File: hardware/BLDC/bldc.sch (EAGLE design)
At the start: 84 parts, among them J1 PWR_2_XT30PW-M, J2 LINEAR_3_JST_PH_RA, J3 LINEAR_8_JST_PH_RA, U1 MA702, U10 MCP2542FD, U11 LDFM33PUR, U2 DRV8323RS, U3 TPN7R006PL, U4 TPN7R006PL, U5 TPN7R006PL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

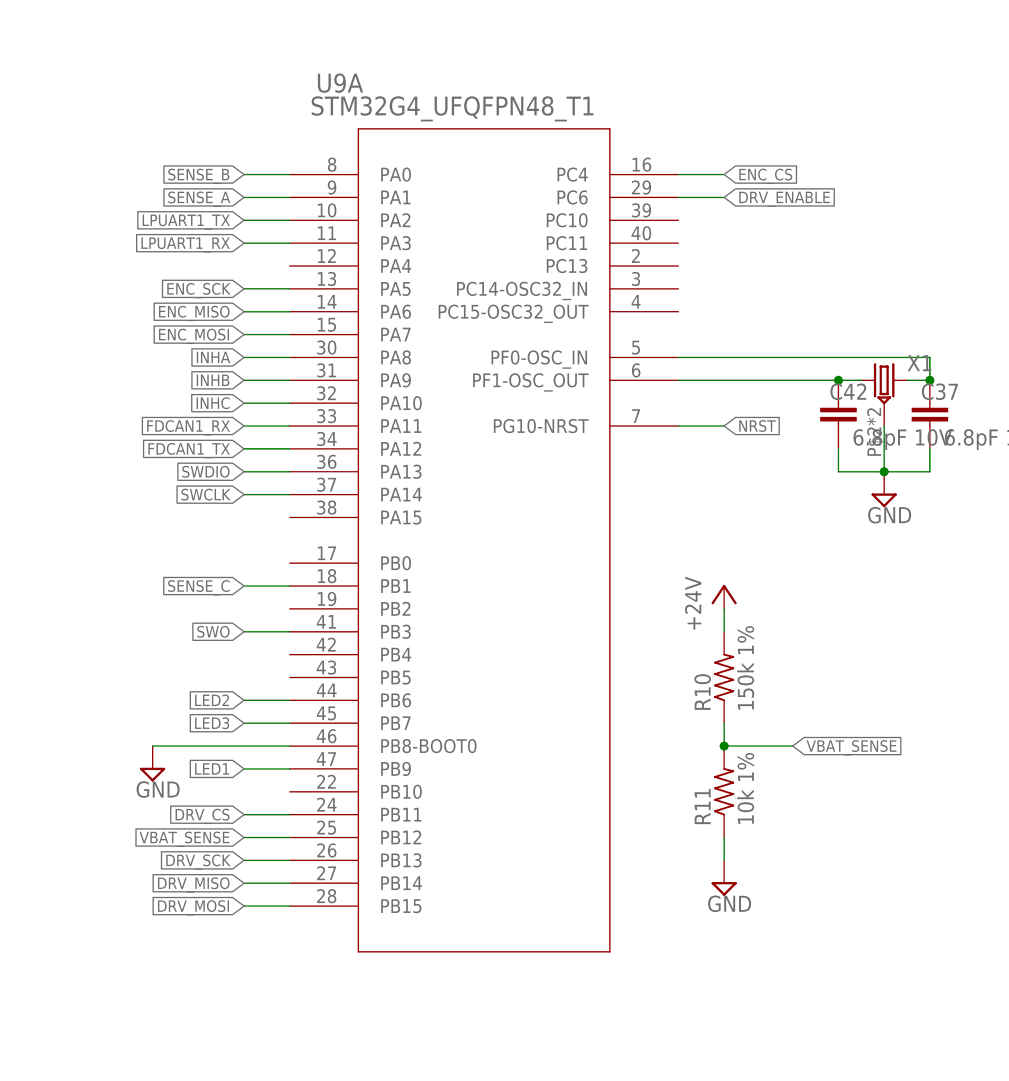
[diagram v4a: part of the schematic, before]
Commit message: SPI2>SPI3. Added cap on nRST
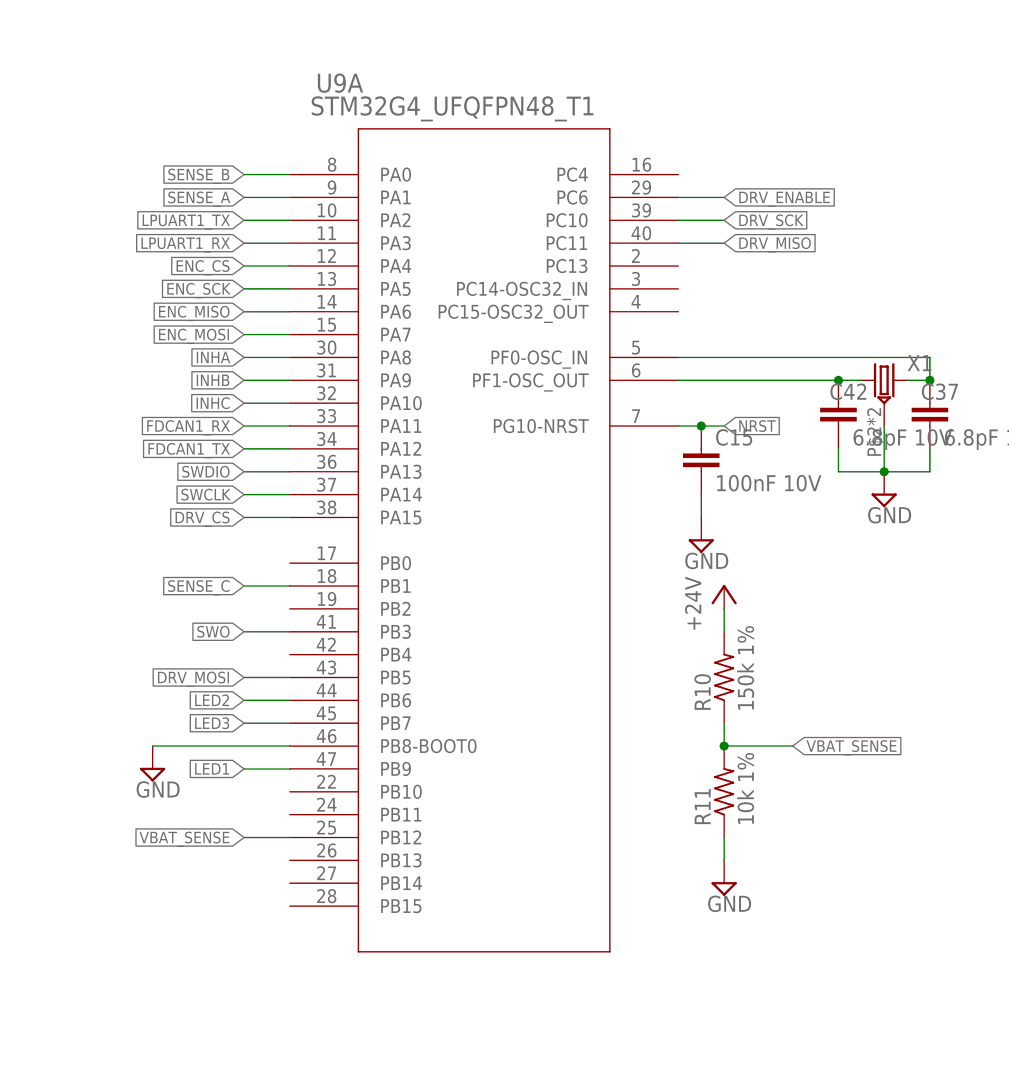
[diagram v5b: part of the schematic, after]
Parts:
- added C15: 100nF 10V, _T_rcl:C0402
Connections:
- net DRV_CS: now also U9A.PA15; no longer U9A.PB11
- net DRV_MISO: now also U9A.PC11; no longer U9A.PB14
- net DRV_MOSI: now also U9A.PB5; no longer U9A.PB15
- net DRV_SCK: now also U9A.PC10; no longer U9A.PB13
- net ENC_CS: now also U9A.PA4; no longer U9A.PC4
- net GND: now also C15.2
- net NRST: now also C15.1
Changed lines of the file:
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@@
 <part name="GND3" library="_T_power" library_urn="urn:adsk.eagle:library:19572085" deviceset="GND" device=""/>
 <part name="GND29" library="_T_power" library_urn="urn:adsk.eagle:library:19572085" deviceset="GND" device=""/>
+<part name="C15" library="_T_rcl" library_urn="urn:adsk.eagle:library:19571919" deviceset="C" device="0402" package3d_urn="urn:adsk.eagle:package:19572013/4" value="100nF 10V"/>
+<part name="GND30" library="_T_power" library_urn="urn:adsk.eagle:library:19572085" deviceset="GND" device=""/>
 </parts>
 <sheets>
@@
 <instance part="GND29" gate="G$1" x="-73.66" y="58.42" smashed="yes" grouprefs="UC_STM32G4">
 <attribute name="VALUE" x="-75.565" y="55.245" size="1.778" layer="96"/>
+</instance>
+<instance part="C15" gate="G$1" x="-12.7" y="93.98" smashed="yes">
+<attribute name="NAME" x="-11.176" y="94.361" size="1.778" layer="95"/>
+<attribute name="VALUE" x="-11.176" y="89.281" size="1.778" layer="96"/>
+</instance>
+<instance part="GND30" gate="G$1" x="-12.7" y="83.82" smashed="yes">
+<attribute name="VALUE" x="-14.605" y="80.645" size="1.778" layer="96"/>
 </instance>
 </instances>
@@
 <net name="DRV_MOSI" class="0">
 <segment>
-<pinref part="U9" gate="A" pin="PB15"/>
-<wire x1="-58.42" y1="43.18" x2="-63.5" y2="43.18" width="0.1524" layer="91" grouprefs="UC_STM32G4"/>
-<label x="-63.5" y="43.18" size="1.27" layer="95" rot="R180" xref="yes" grouprefs="UC_STM32G4"/>
-</segment>
-<segment>
 <pinref part="U2" gate="G$1" pin="SDI"/>
 <wire x1="101.6" y1="91.44" x2="99.06" y2="91.44" width="0.1524" layer="91" grouprefs="GATE_DRIVER_DRV8323RS"/>
 <label x="99.06" y="91.44" size="1.27" layer="95" rot="R180" xref="yes" grouprefs="GATE_DRIVER_DRV8323RS"/>
 </segment>
+<segment>
+<pinref part="U9" gate="A" pin="PB5"/>
+<wire x1="-58.42" y1="68.58" x2="-63.5" y2="68.58" width="0.1524" layer="91"/>
+<label x="-63.5" y="68.58" size="1.27" layer="95" rot="R180" xref="yes"/>
+</segment>
 </net>
 <net name="DRV_MISO" class="0">
-<segment>
-<pinref part="U9" gate="A" pin="PB14"/>
-<wire x1="-58.42" y1="45.72" x2="-63.5" y2="45.72" width="0.1524" layer="91" grouprefs="UC_STM32G4"/>
-<label x="-63.5" y="45.72" size="1.27" layer="95" rot="R180" xref="yes" grouprefs="UC_STM32G4"/>
-</segment>
 <segment>
 <pinref part="U2" gate="G$1" pin="SDO"/>
@@
 <junction x="81.28" y="88.9" grouprefs="GATE_DRIVER_DRV8323RS"/>
 </segment>
+<segment>
+<pinref part="U9" gate="A" pin="PC11"/>
+<wire x1="-15.24" y1="116.84" x2="-10.16" y2="116.84" width="0.1524" layer="91"/>
+<label x="-10.16" y="116.84" size="1.27" layer="95" xref="yes"/>
+</segment>
 </net>
 <net name="DRV_SCK" class="0">
-<segment>
-<pinref part="U9" gate="A" pin="PB13"/>
-<wire x1="-58.42" y1="48.26" x2="-63.5" y2="48.26" width="0.1524" layer="91" grouprefs="UC_STM32G4"/>
-<label x="-63.5" y="48.26" size="1.27" layer="95" rot="R180" xref="yes" grouprefs="UC_STM32G4"/>
-</segment>
 <segment>
 <pinref part="U2" gate="G$1" pin="SCLK"/>
@@
 <label x="99.06" y="86.36" size="1.27" layer="95" rot="R180" xref="yes" grouprefs="GATE_DRIVER_DRV8323RS"/>
 </segment>
+<segment>
+<pinref part="U9" gate="A" pin="PC10"/>
+<wire x1="-15.24" y1="119.38" x2="-10.16" y2="119.38" width="0.1524" layer="91"/>
+<label x="-10.16" y="119.38" size="1.27" layer="95" xref="yes"/>
+</segment>
 </net>
 <net name="DRV_CS" class="0">
@@
 </segment>
 <segment>
-<pinref part="U9" gate="A" pin="PB11"/>
-<wire x1="-58.42" y1="53.34" x2="-63.5" y2="53.34" width="0.1524" layer="91" grouprefs="UC_STM32G4"/>
-<label x="-63.5" y="53.34" size="1.27" layer="95" rot="R180" xref="yes" grouprefs="UC_STM32G4"/>
+<pinref part="U9" gate="A" pin="PA15"/>
+<wire x1="-58.42" y1="86.36" x2="-63.5" y2="86.36" width="0.1524" layer="91"/>
+<label x="-63.5" y="86.36" size="1.27" layer="95" rot="R180" xref="yes"/>
 </segment>
 </net>
 <net name="ENC_CS" class="0">
-<segment>
-<pinref part="U9" gate="A" pin="PC4"/>
-<wire x1="-15.24" y1="124.46" x2="-10.16" y2="124.46" width="0.1524" layer="91" grouprefs="UC_STM32G4"/>
-<label x="-10.16" y="124.46" size="1.27" layer="95" xref="yes" grouprefs="UC_STM32G4"/>
-</segment>
 <segment>
 <pinref part="U1" gate="G$1" pin="CS"/>
 <wire x1="185.42" y1="-5.08" x2="182.88" y2="-5.08" width="0.1524" layer="91" grouprefs="MAG_SENSE"/>
 <label x="182.88" y="-5.08" size="1.27" layer="95" rot="R180" xref="yes" grouprefs="MAG_SENSE"/>
+</segment>
+<segment>
+<pinref part="U9" gate="A" pin="PA4"/>
+<wire x1="-58.42" y1="114.3" x2="-63.5" y2="114.3" width="0.1524" layer="91"/>
+<label x="-63.5" y="114.3" size="1.27" layer="95" rot="R180" xref="yes"/>
 </segment>
 </net>
@@
 <wire x1="-58.42" y1="60.96" x2="-73.66" y2="60.96" width="0.1524" layer="91" grouprefs="UC_STM32G4"/>
 </segment>
+<segment>
+<pinref part="GND30" gate="G$1" pin="GND"/>
+<pinref part="C15" gate="G$1" pin="2"/>
+<wire x1="-12.7" y1="86.36" x2="-12.7" y2="88.9" width="0.1524" layer="91"/>
+</segment>
 </net>
 <net name="+24V" class="2">
@@
 <net name="DRV_ENABLE" class="0">
 <segment>
-<pinref part="U9" gate="A" pin="PC6"/>
-<wire x1="-15.24" y1="121.92" x2="-10.16" y2="121.92" width="0.1524" layer="91" grouprefs="UC_STM32G4"/>
-<label x="-10.16" y="121.92" size="1.27" layer="95" xref="yes" grouprefs="UC_STM32G4"/>
-</segment>
-<segment>
 <pinref part="U2" gate="G$1" pin="ENABLE"/>
 <wire x1="101.6" y1="114.3" x2="96.52" y2="114.3" width="0.1524" layer="91" grouprefs="GATE_DRIVER_DRV8323RS"/>
@@
 <label x="96.52" y="96.52" size="1.27" layer="95" rot="R180" xref="yes" grouprefs="GATE_DRIVER_DRV8323RS"/>
 </segment>
+<segment>
+<pinref part="U9" gate="A" pin="PC6"/>
+<wire x1="-15.24" y1="121.92" x2="-10.16" y2="121.92" width="0.1524" layer="91"/>
+<label x="-10.16" y="121.92" size="1.27" layer="95" xref="yes"/>
+</segment>
 </net>
 <net name="SHA" class="0">
@@
 <segment>
 <pinref part="U9" gate="A" pin="PG10-NRST"/>
-<wire x1="-15.24" y1="96.52" x2="-10.16" y2="96.52" width="0.1524" layer="91" grouprefs="UC_STM32G4"/>
+<wire x1="-15.24" y1="96.52" x2="-12.7" y2="96.52" width="0.1524" layer="91" grouprefs="UC_STM32G4"/>
 <label x="-10.16" y="96.52" size="1.27" layer="95" xref="yes" grouprefs="UC_STM32G4"/>
-</segment>
-<segment>
+<pinref part="C15" gate="G$1" pin="1"/>
+<wire x1="-12.7" y1="96.52" x2="-10.16" y2="96.52" width="0.1524" layer="91" grouprefs="UC_STM32G4"/>
+<junction x="-12.7" y="96.52"/>
+</segment>
+<segment>

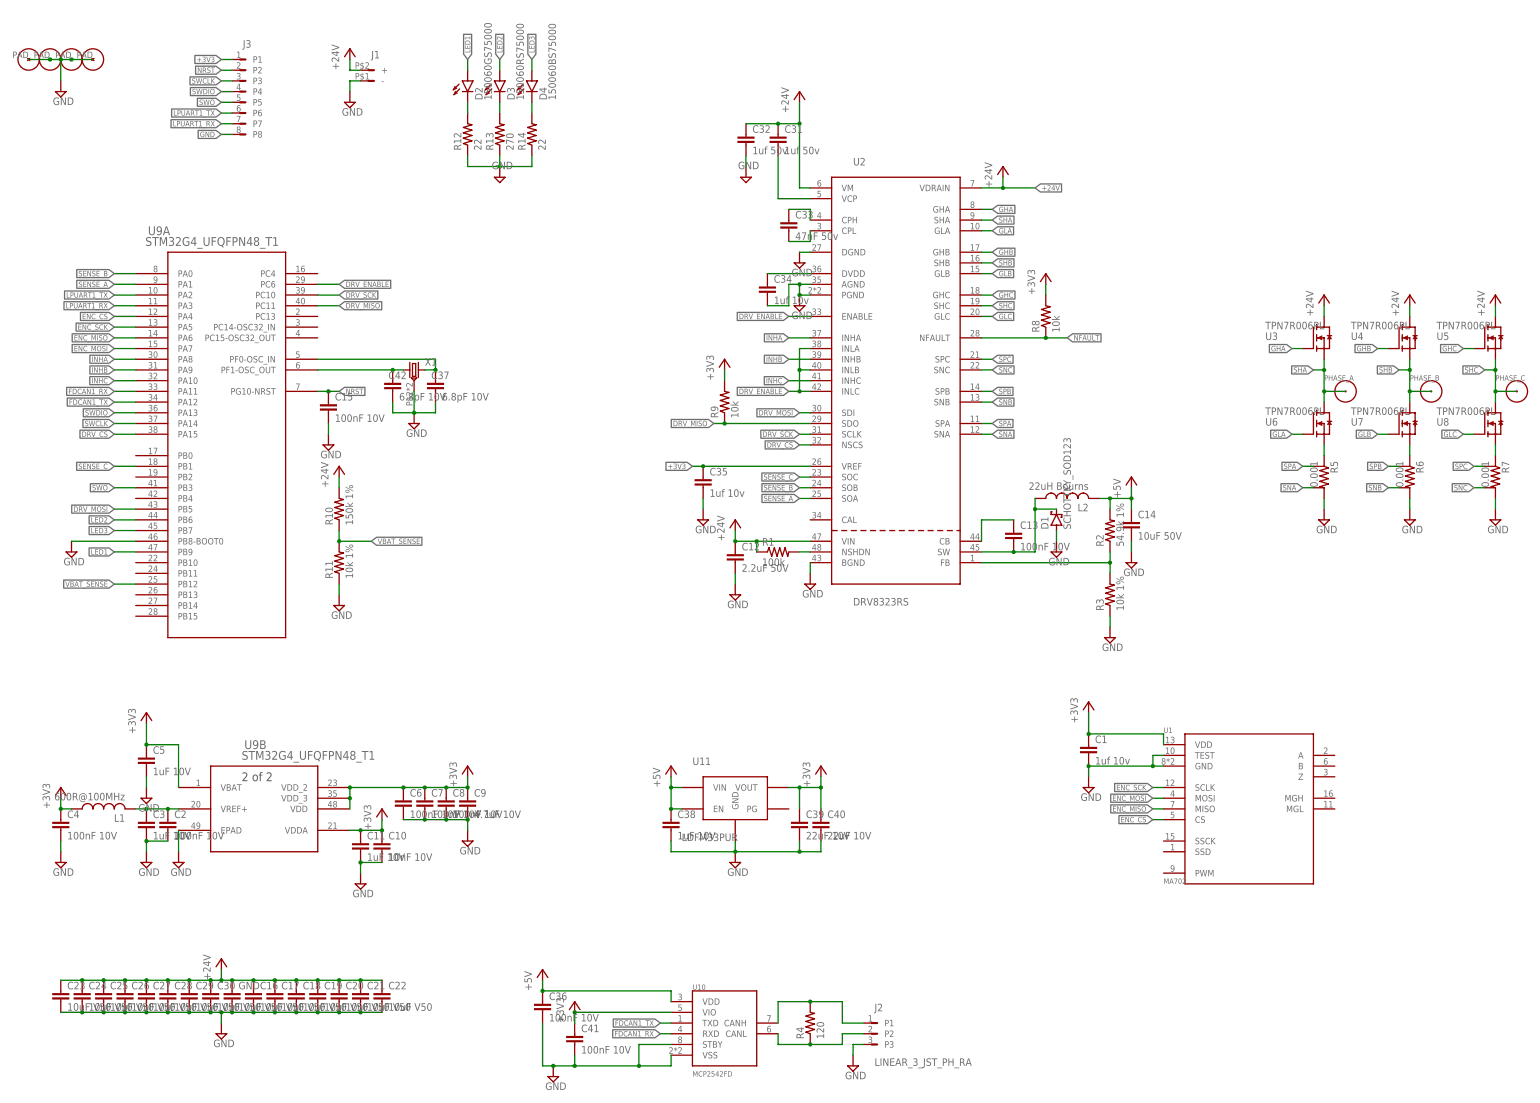
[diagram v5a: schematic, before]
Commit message: Added filtering to VDDA
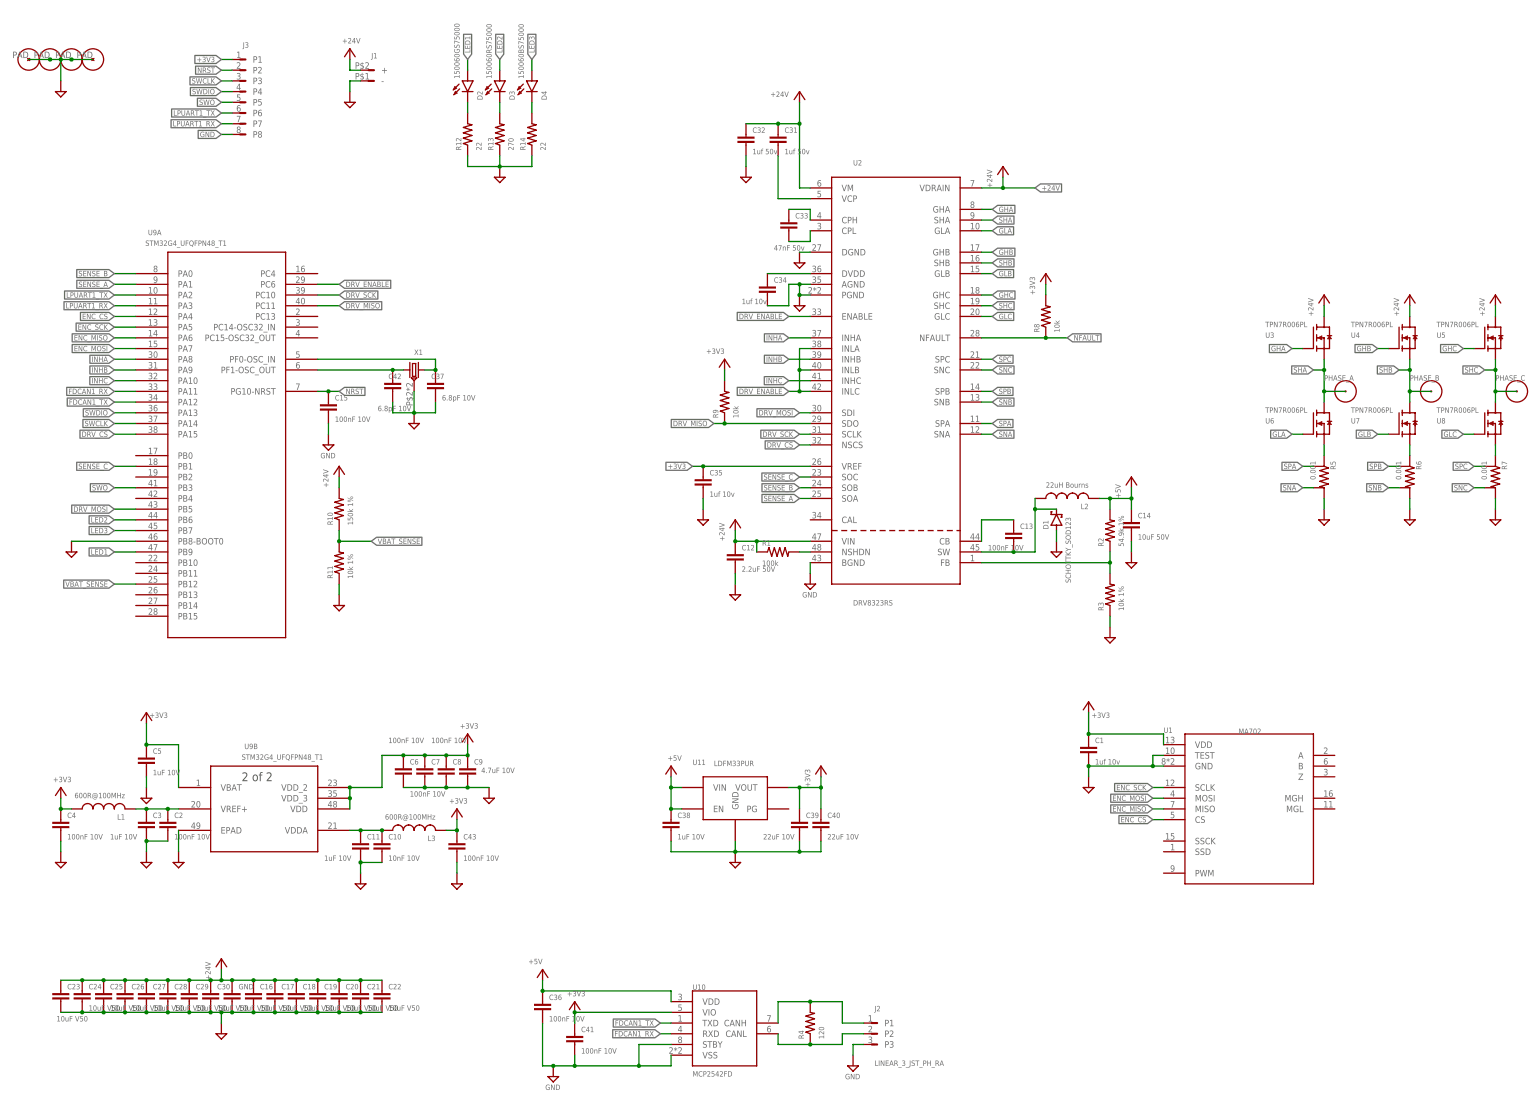
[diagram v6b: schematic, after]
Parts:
- added C43: 100nF 10V, _T_rcl:C0402
- added L3: 600R@100MHz, _T_rcl:DC_CHOKE_FERRITE_BEAD_0603
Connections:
- new net N$16: C10.1, C11.1, L3.1, U9B.VDDA
- net +3V3: now also C43.1, L3.2; no longer C10.1, C11.1, U9B.VDDA
- net GND: now also C43.2
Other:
- moved on the sheet: C6, C7, C8, C9

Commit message: Fixed labels
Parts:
- removed GND: 10uF V50, _T_rcl:C1206
- added C44: 10uF 50V, _T_rcl:C1206
- C16, C17, C18, C19, C20, C21, C22, C23, C24, C25, C26, C27, C28, C29, C30: value 10uF V50 -> 10uF 50V
- C39, C40: value 22uF 10V -> 2.2uF 10V
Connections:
- net +24V: now also C44.1; no longer GND.1
- net GND: now also C44.2; no longer GND.2
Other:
- moved on the sheet: C1, C16, C17, C18, C19, C20, C21, C22, C23, C24, C25, C26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
